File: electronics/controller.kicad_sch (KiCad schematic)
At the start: 70 parts, among them J1 Conn_01x02, J10 Heated_Bed_Thermistor_Connect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, J11 Bl_Touch_Gnd_ZMin_Connector, J12 Bl_Touch_Signal_Vcc_Gnd_Conne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, J13 Motor_A_Connector, J14 Motor_B_Connector, J15 Motor_Z_Connector, J16 Motor_E_Connector, J2 X_Axis_Endstop_Connector, J3 Y_Axis_Endstop_Connector, J4 USB_C_Receptacle_USB2.0, J5 Hotend_Connector, J6 Heated_Bed_Connector, J7 Hotend_Fan_Connector, J8 Layer_Fan_Connector, J9 Hotend_Thermistor_Connector, Q1 PSMN4R1-30YLC, Q2 PSMN4R1-30YLC, Q3 PSMN4R1-30YLC, Q4 PSMN4R1-30YLC, SW1 EN_Button, SW2 Boot_Button, SW3 Pause/Resume_Button, U1 K7803JT-500R3-LB, U2 LMTOE78_05-0.5, U3 ESP32-S3-WROOM-1, U4 MT29F2G01ABAGDWB-IT, U5 USBLC6-2SC6, U6 TMC2209_SILENTSTEPSTICK, U7 TMC2209_SILENTSTEPSTICK, U8 TMC2209_SILENTSTEPSTICK, U9 TMC2209_SILENTSTEPSTICK

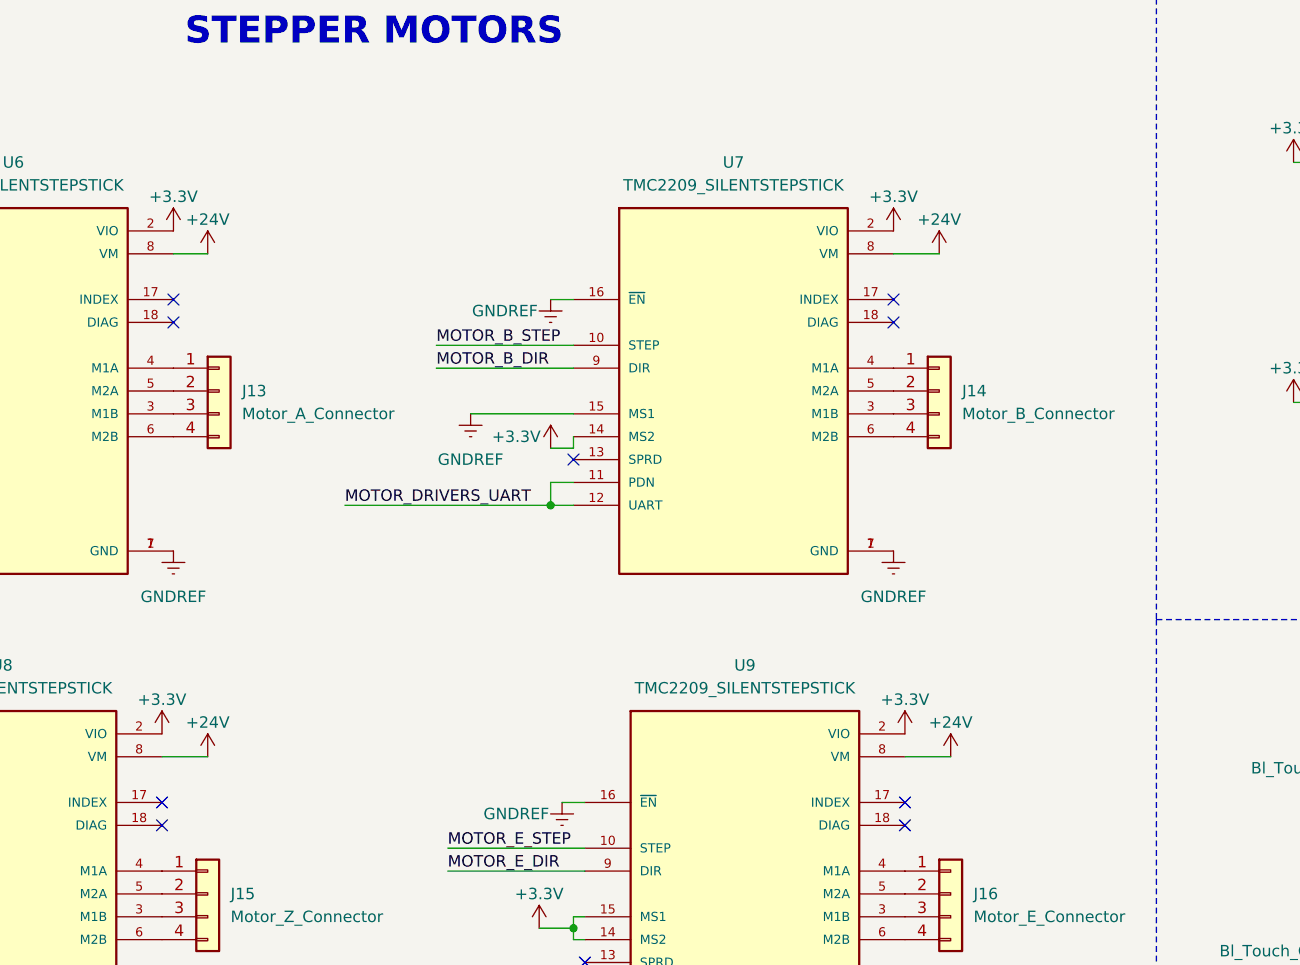
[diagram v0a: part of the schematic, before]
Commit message: ⚡️ Add bulking capacitors for stepper motors on KiCad schematic
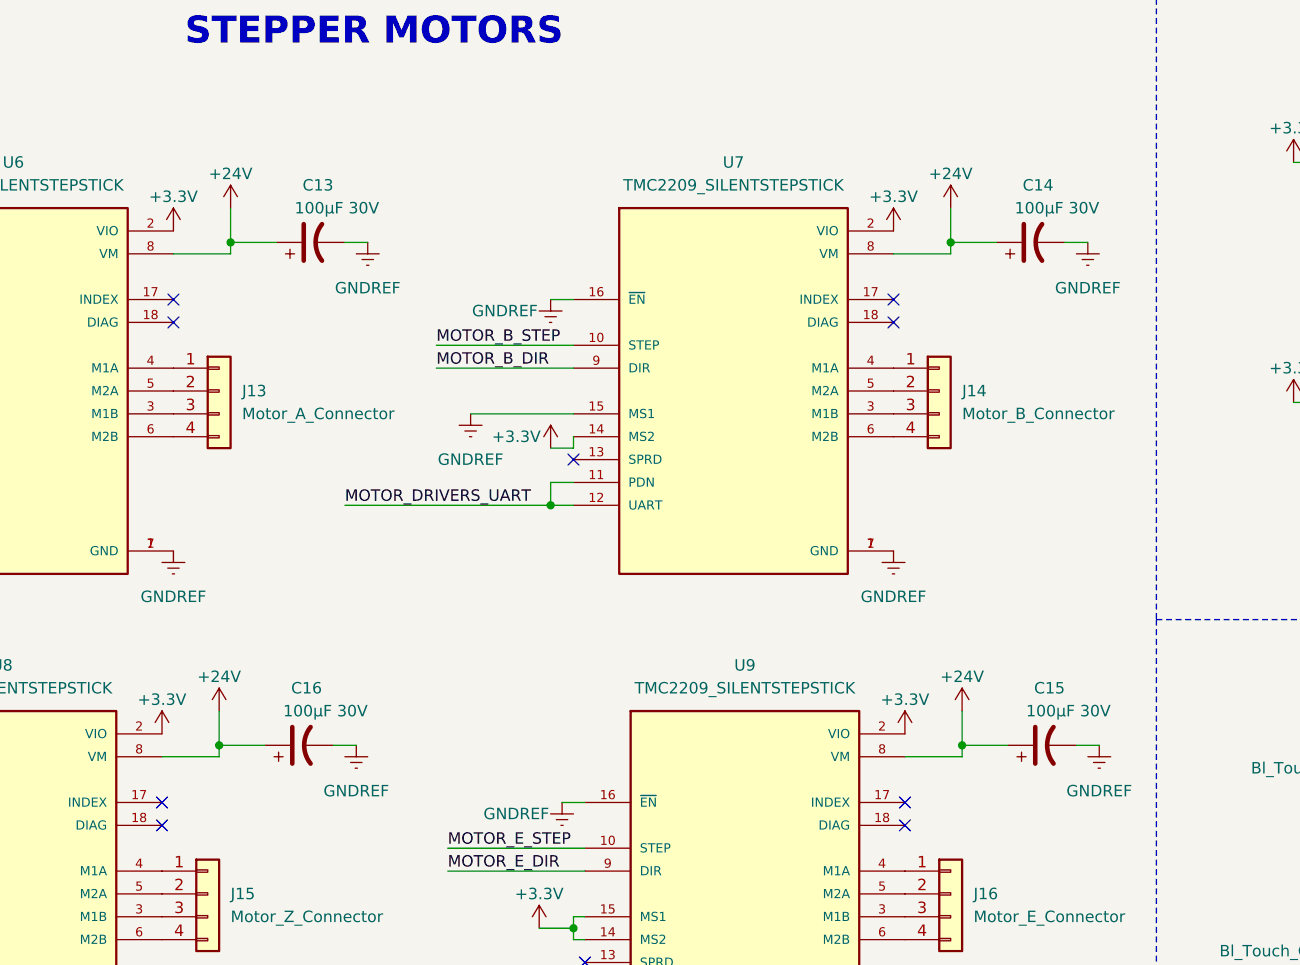
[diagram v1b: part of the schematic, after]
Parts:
- added C13, C14, C15, C16: 100µF 30V, symbol Project:C_Polarized_US
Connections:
- net +24V: now also C13.1, C14.1, C15.1, C16.1
- net GNDREF: now also C13.2, C14.2, C15.2, C16.2

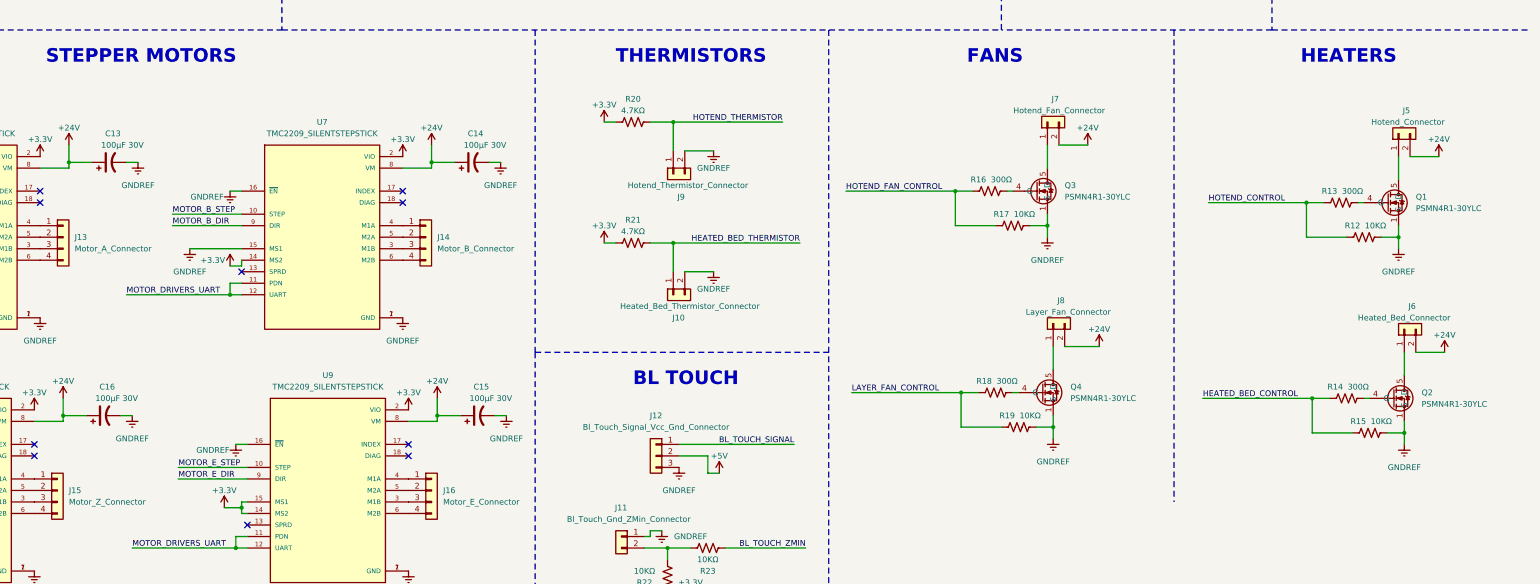
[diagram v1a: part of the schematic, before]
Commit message: ⚡️ Add capacitors for fans, heating elements, BLTouch on KiCad schematic
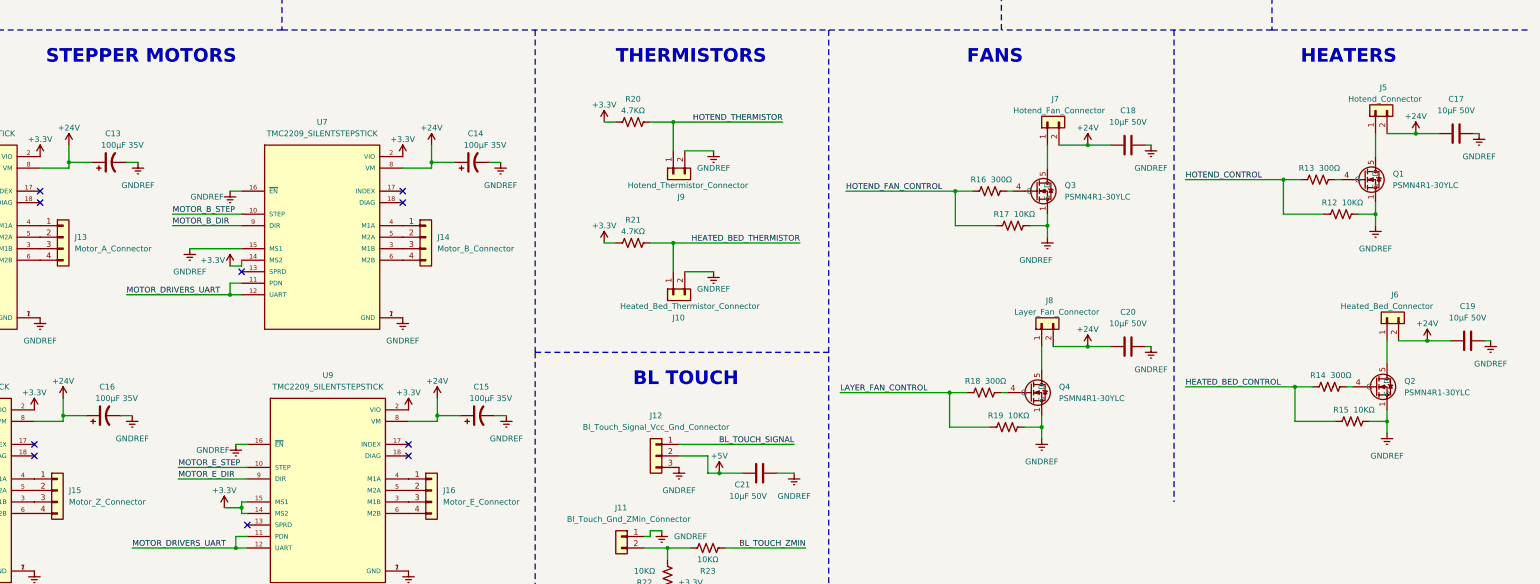
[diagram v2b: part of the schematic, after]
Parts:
- added C17, C18, C19, C20, C21: 10µF 50V, symbol Project:C
- C13, C14, C15, C16: value 100µF 30V -> 100µF 35V
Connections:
- net +24V: now also C17.1, C18.1, C19.1, C20.1
- net +5V: now also C21.1
- net GNDREF: now also C17.2, C18.2, C19.2, C20.2, C21.2
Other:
- moved on the sheet: J5, J6, J8, Q1, Q2, Q4, R12, R13, R14, R15, R18, R19

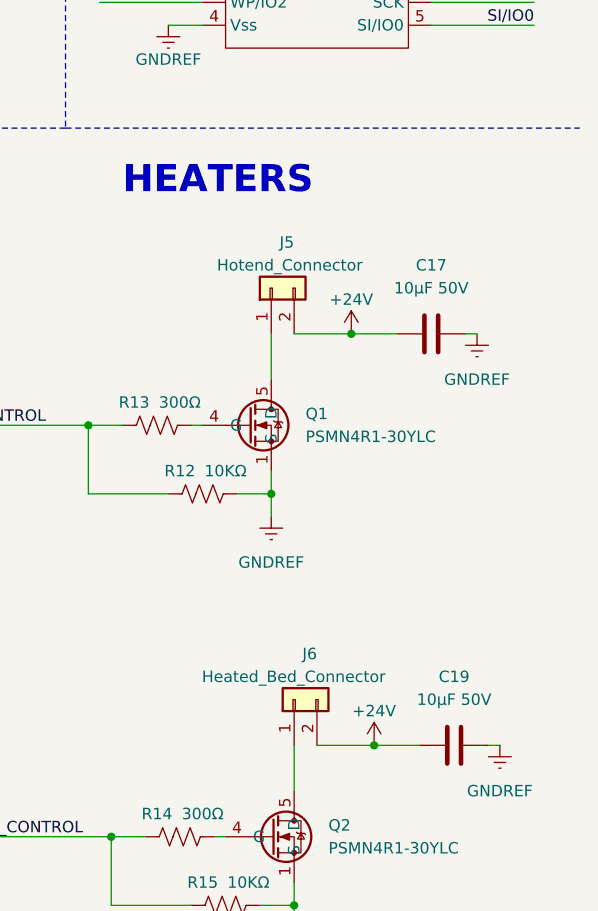
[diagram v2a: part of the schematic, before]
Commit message: ✨ Add overcurrent protection to heaters on KiCad schematic
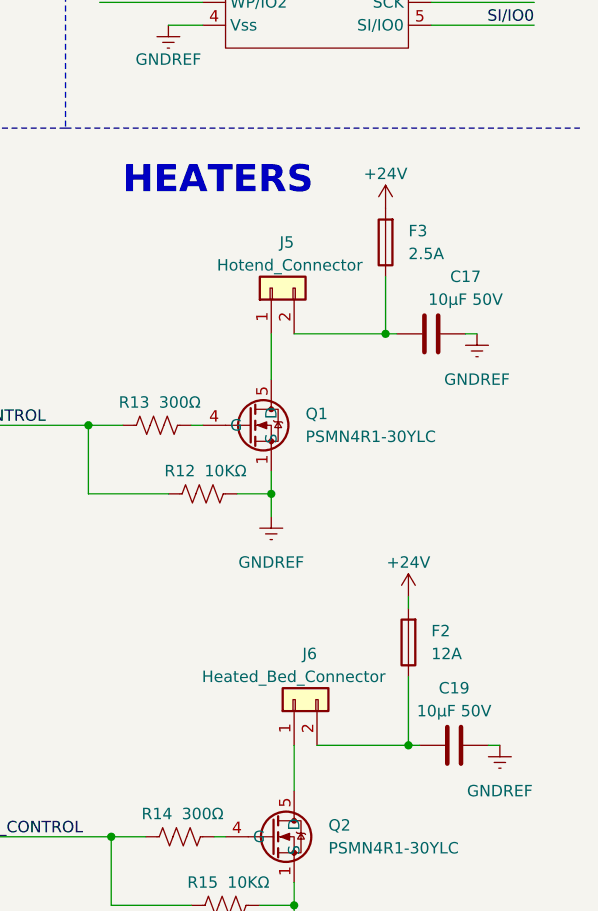
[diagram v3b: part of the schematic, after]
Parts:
- added F2: 12A, symbol Project:Fuse
- added F3: 2.5A, symbol Project:Fuse
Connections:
- net +24V: now also F2.2, F3.2; no longer C17.1, C19.1, J5.2 (Pin_2), J6.2 (Pin_2)
- new net: C17.1, F3.1, J5.2 (Pin_2)
- new net: C19.1, F2.1, J6.2 (Pin_2)
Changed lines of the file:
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@@
   (junction (at 331.47 34.29) (diameter 0) (color 0 0 0 0)
   )
+  (junction (at 387.35 172.72) (diameter 0) (color 0 0 0 0)
+  )
   (junction (at 307.34 83.82) (diameter 0) (color 0 0 0 0)
   )
@@
   (junction (at 119.38 121.92) (diameter 0) (color 0 0 0 0)
   )
-  (junction (at 383.54 172.72) (diameter 0) (color 0 0 0 0)
-  )
   (junction (at 222.25 31.75) (diameter 0) (color 0 0 0 0)
   )
@@
   (junction (at 161.29 43.18) (diameter 0) (color 0 0 0 0)
   )
+  (junction (at 389.89 218.44) (diameter 0) (color 0 0 0 0)
+  )
   (junction (at 365.76 130.81) (diameter 0) (color 0 0 0 0)
   )
@@
   (junction (at 383.54 49.53) (diameter 0) (color 0 0 0 0)
   )
-  (junction (at 386.08 218.44) (diameter 0) (color 0 0 0 0)
-  )
   (junction (at 265.43 106.68) (diameter 0) (color 0 0 0 0)
   )
@@
     (stroke (width 0) (type dash))
   )
+  (wire (pts (xy 389.89 218.44) (xy 391.16 218.44))
+    (stroke (width 0) (type default))
+  )
   (polyline (pts (xy 189.23 220.98) (xy 189.23 285.75))
     (stroke (width 0) (type dash))
@@
     (stroke (width 0) (type default))
   )
+  (wire (pts (xy 389.89 210.82) (xy 389.89 218.44))
+    (stroke (width 0) (type default))
+  )
   (wire (pts (xy 256.54 76.2) (xy 283.21 76.2))
     (stroke (width 0) (type default))
@@
     (stroke (width 0) (type default))
   )
+  (wire (pts (xy 389.89 201.93) (xy 389.89 203.2))
+    (stroke (width 0) (type default))
+  )
   (wire (pts (xy 34.29 49.53) (xy 45.72 49.53))
     (stroke (width 0) (type default))
@@
     (stroke (width 0) (type default))
   )
+  (wire (pts (xy 387.35 166.37) (xy 387.35 172.72))
+    (stroke (width 0) (type default))
+  )
   (wire (pts (xy 214.63 170.18) (xy 219.71 170.18))
     (stroke (width 0) (type default))
@@
     (stroke (width 0) (type default))
   )
+  (wire (pts (xy 387.35 172.72) (xy 388.62 172.72))
+    (stroke (width 0) (type default))
+  )
   (wire (pts (xy 156.21 43.18) (xy 161.29 43.18))
     (stroke (width 0) (type default))
@@
     (stroke (width 0) (type default))
   )
-  (wire (pts (xy 383.54 172.72) (xy 388.62 172.72))
-    (stroke (width 0) (type default))
-  )
   (wire (pts (xy 256.54 106.68) (xy 265.43 106.68))
     (stroke (width 0) (type default))
@@
     (stroke (width 0) (type default))
   )
-  (wire (pts (xy 386.08 218.44) (xy 379.73 218.44))
-    (stroke (width 0) (type default))
-  )
   (wire (pts (xy 312.42 40.64) (xy 318.77 40.64))
     (stroke (width 0) (type default))
@@
     (stroke (width 0) (type default))
   )
-  (wire (pts (xy 383.54 172.72) (xy 377.19 172.72))
+  (wire (pts (xy 377.19 172.72) (xy 387.35 172.72))
     (stroke (width 0) (type default))
   )
@@
     (stroke (width 0) (type default))
   )
-  (wire (pts (xy 386.08 218.44) (xy 391.16 218.44))
+  (wire (pts (xy 379.73 218.44) (xy 389.89 218.44))
     (stroke (width 0) (type default))
   )
@@
   )
   (symbol (lib_id "Project:C") (at 392.43 172.72 90) (unit 1)
-    (in_bom yes) (on_board yes) (dnp no) (fields_autoplaced)
-    (property "Reference" "C17" (at 392.43 165.1 90)
+    (in_bom yes) (on_board yes) (dnp no)
+    (property "Reference" "C17" (at 396.24 166.37 90)
       (effects (font (size 1.27 1.27)))
     )
-    (property "Value" "10µF 50V" (at 392.43 167.64 90)
+    (property "Value" "10µF 50V" (at 396.24 168.91 90)
       (effects (font (size 1.27 1.27)))
     )
@@
   )
   (symbol (lib_id "Project:C") (at 394.97 218.44 90) (unit 1)
-    (in_bom yes) (on_board yes) (dnp no) (fields_autoplaced)
-    (property "Reference" "C19" (at 394.97 210.82 90)
+    (in_bom yes) (on_board yes) (dnp no)
+    (property "Reference" "C19" (at 394.97 212.09 90)
       (effects (font (size 1.27 1.27)))
     )
-    (property "Value" "10µF 50V" (at 394.97 213.36 90)
+    (property "Value" "10µF 50V" (at 394.97 214.63 90)
       (effects (font (size 1.27 1.27)))
     )
@@
     )
   )
+  (symbol (lib_id "Project:Fuse") (at 389.89 207.01 180) (unit 1)
+    (in_bom yes) (on_board yes) (dnp no) (fields_autoplaced)
+    (property "Reference" "F2" (at 392.43 205.74 0)
+      (effects (font (size 1.27 1.27)) (justify right))
+    )
+    (property "Value" "12A" (at 392.43 208.28 0)
+      (effects (font (size 1.27 1.27)) (justify right))
+    )
+    (property "Footprint" "" (at 391.668 207.01 90)
+      (effects (font (size 1.27 1.27)) hide)
+    )
+    (property "Datasheet" "~" (at 389.89 207.01 0)
+      (effects (font (size 1.27 1.27)) hide)
+    )
+    (pin "1")
+    (pin "2")
+    (instances
+      (project "controller"
+        (path "/b72cfb6e-763f-4aec-88af-02f682ab9e2d"
+          (reference "F2") (unit 1)
+        )
+      )
+    )
+  )
   (symbol (lib_id "Project:R_US") (at 361.95 182.88 90) (unit 1)
     (in_bom yes) (on_board yes) (dnp no)
@@
     )
   )
+  (symbol (lib_id "Project:Fuse") (at 387.35 162.56 180) (unit 1)
+    (in_bom yes) (on_board yes) (dnp no) (fields_autoplaced)
+    (property "Reference" "F3" (at 389.89 161.29 0)
+      (effects (font (size 1.27 1.27)) (justify right))
+    )
+    (property "Value" "2.5A" (at 389.89 163.83 0)
+      (effects (font (size 1.27 1.27)) (justify right))
+    )
+    (property "Footprint" "" (at 389.128 162.56 90)
+      (effects (font (size 1.27 1.27)) hide)
+    )
+    (property "Datasheet" "~" (at 387.35 162.56 0)
+      (effects (font (size 1.27 1.27)) hide)
+    )
+    (pin "1")
+    (pin "2")
+    (instances
+      (project "controller"
+        (path "/b72cfb6e-763f-4aec-88af-02f682ab9e2d"
+          (reference "F3") (unit 1)
+        )
+      )
+    )
+  )
   (symbol (lib_id "Project:K7803JT-500R3-LB") (at 95.25 33.02 0) (unit 1)
     (in_bom yes) (on_board yes) (dnp no)
@@
     )
   )
-  (symbol (lib_id "Project:+24V") (at 383.54 172.72 0) (unit 1)
+  (symbol (lib_id "Project:+24V") (at 387.35 158.75 0) (unit 1)
     (in_bom yes) (on_board yes) (dnp no)
-    (property "Reference" "#PWR039" (at 383.54 176.53 0)
+    (property "Reference" "#PWR039" (at 387.35 162.56 0)
       (effects (font (size 1.27 1.27)) hide)
     )
-    (property "Value" "+24V" (at 383.54 168.91 0)
+    (property "Value" "+24V" (at 387.35 154.94 0)
       (effects (font (size 1.27 1.27)))
     )
-    (property "Footprint" "" (at 383.54 172.72 0)
+    (property "Footprint" "" (at 387.35 158.75 0)
       (effects (font (size 1.27 1.27)) hide)
     )
-    (property "Datasheet" "" (at 383.54 172.72 0)
+    (property "Datasheet" "" (at 387.35 158.75 0)
       (effects (font (size 1.27 1.27)) hide)
     )
@@
     )
   )
-  (symbol (lib_id "Project:+24V") (at 386.08 218.44 0) (unit 1)
+  (symbol (lib_id "Project:+24V") (at 389.89 201.93 0) (unit 1)
     (in_bom yes) (on_board yes) (dnp no)
-    (property "Reference" "#PWR041" (at 386.08 222.25 0)
+    (property "Reference" "#PWR041" (at 389.89 205.74 0)
       (effects (font (size 1.27 1.27)) hide)
     )
-    (property "Value" "+24V" (at 386.08 214.63 0)
+    (property "Value" "+24V" (at 389.89 198.12 0)
       (effects (font (size 1.27 1.27)))
     )
-    (property "Footprint" "" (at 386.08 218.44 0)
+    (property "Footprint" "" (at 389.89 201.93 0)
       (effects (font (size 1.27 1.27)) hide)
     )
-    (property "Datasheet" "" (at 386.08 218.44 0)
+    (property "Datasheet" "" (at 389.89 201.93 0)
       (effects (font (size 1.27 1.27)) hide)
     )
